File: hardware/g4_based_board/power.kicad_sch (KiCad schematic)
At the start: 10 parts, among them U2 AZ1117-3.3

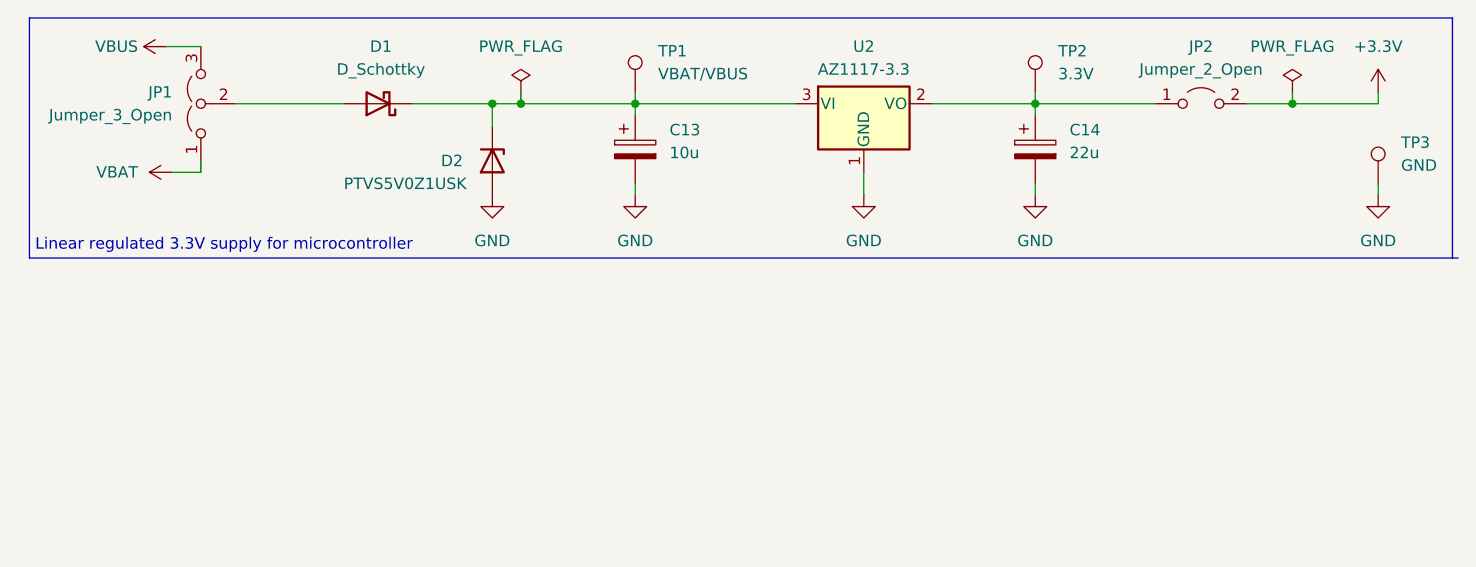
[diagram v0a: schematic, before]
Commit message: added a 5v linear reg
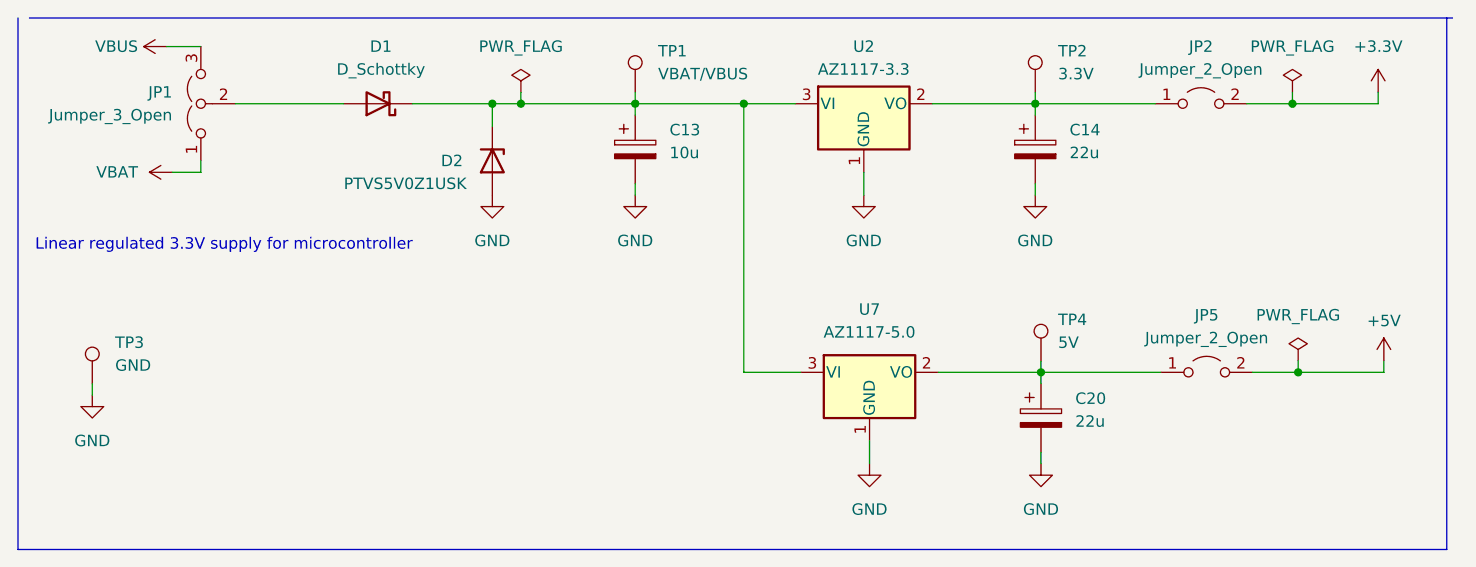
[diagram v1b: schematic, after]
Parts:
- added C20: 22u, Capacitor_SMD:C_0805_2012Metric, symbol Device:C_Polarized
- added JP5: Jumper_2_Open, symbol Jumper:Jumper_2_Open
- added TP4: 5V, TestPoint:TestPoint_Pad_D1.5mm, symbol Connector:TestPoint
- added U7: AZ1117-5.0, symbol Regulator_Linear:AZ1117-5.0
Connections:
- net GND: now also C20.2, U7.1 (GND)
- net at C13.1, D1.1 (K), D2.1 (K)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: now also U7.3 (VI)
- new net: C20.1, JP5.1 (A), TP4.1, U7.2 (VO)
- new net +5V: JP5.2 (B)
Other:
- moved on the sheet: TP3

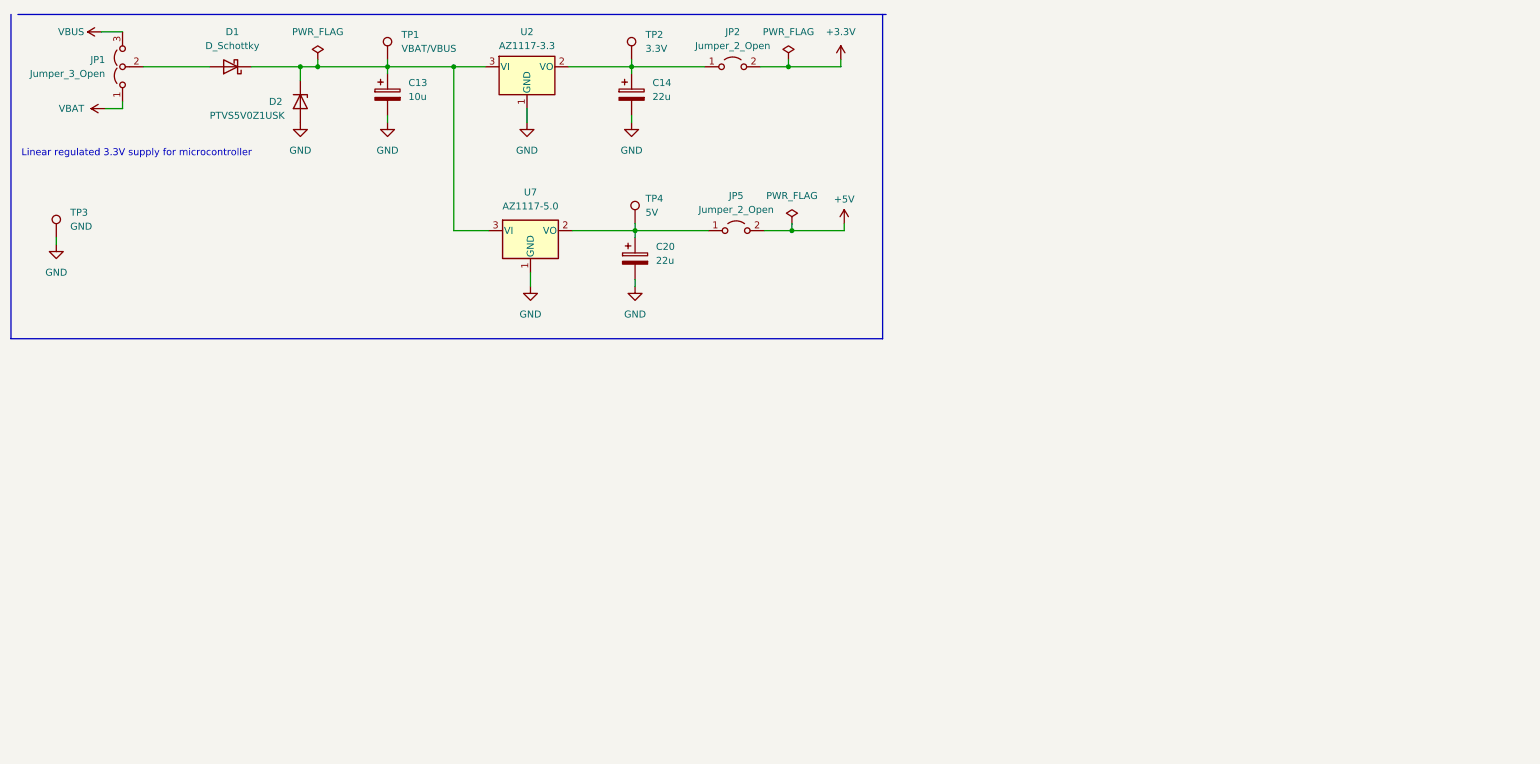
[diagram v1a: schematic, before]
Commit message: moved the 5v reg to only use the battery as input
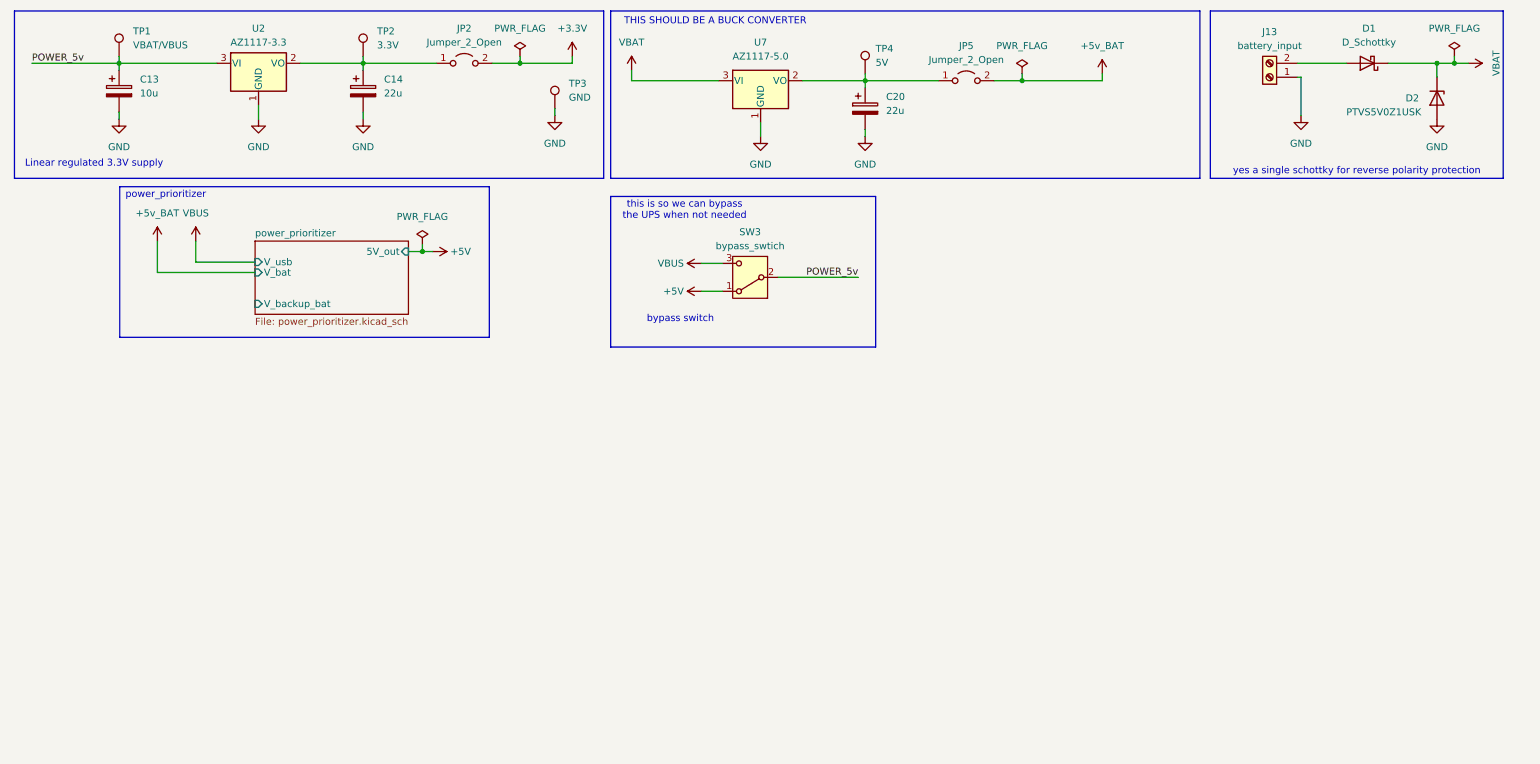
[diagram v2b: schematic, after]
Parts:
- removed JP1: Jumper_3_Open, Connector_PinHeader_2.54mm:PinHeader_1x03_P2.54mm_Vertical, symbol Jumper:Jumper_3_Open
- added J13: battery_input, symbol Connector:Screw_Terminal_01x02
- added SW3: bypass_swtich, symbol Switch:SW_SPDT
- U7: footprint (none) -> Package_TO_SOT_SMD:SOT-223
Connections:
- net +5V: now also SW3.1 (A); no longer JP5.2 (B)
- net GND: now also J13.1 (Pin_1)
- net VBAT: now also D1.1 (K), D2.1 (K), U7.3 (VI)
- net VBUS: now also SW3.3 (C)
- net POWER_5v: now reaches C13.1, TP1.1, U2.3 (VI)
- net POWER_5v: now also SW3.2 (B); no longer D1.1 (K), D2.1 (K), U7.3 (VI)
- net at D1.2 (A): now also J13.2 (Pin_2)
- new net +5v_BAT: JP5.2 (B)
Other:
- added sheet power_prioritizer (power_prioritizer.kicad_sch)
- note added: "Linear regulated 3.3V supply"
- note added: "THIS SHOULD BE A BUCK CONVERTER"
- note added: "bypass switch"
- note added: "power_prioritizer"
- note added: "this is so we can bypass the UPS when not needed"
- note added: "yes a single schottky for reverse polarity protection"
- note removed: "Linear regulated 3.3V supply for microcontroller"
- moved on the sheet: C13, C14, JP2, TP1, TP2, TP3, U2

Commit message: changed power to be an external module
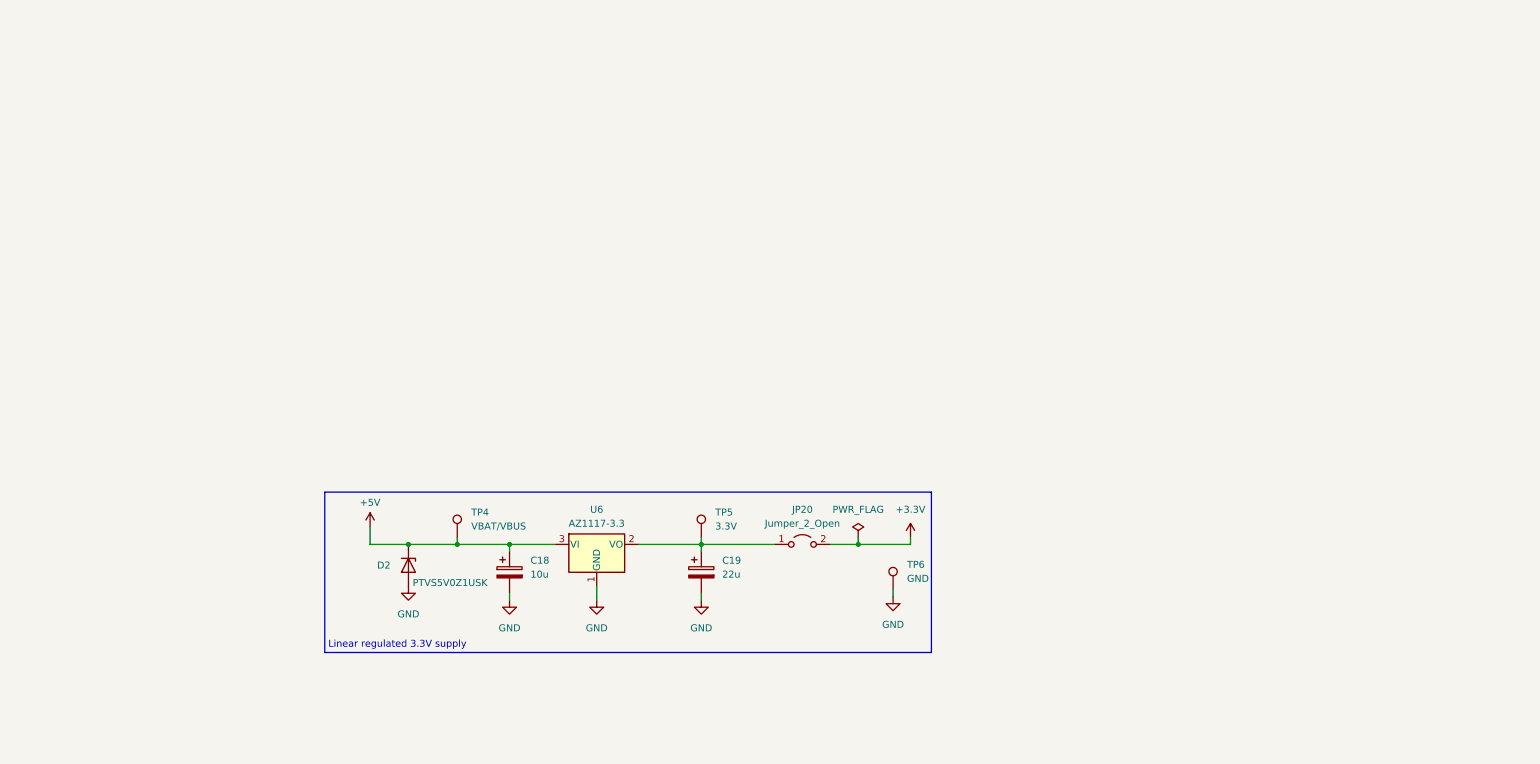
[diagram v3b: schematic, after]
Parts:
- removed C13: 10u, Capacitor_SMD:C_0805_2012Metric, symbol Device:C_Polarized
- removed C14, C20: 22u, Capacitor_SMD:C_0805_2012Metric, symbol Device:C_Polarized
- removed D1: D_Schottky, Diode_SMD:D_0805_2012Metric_Pad1.15x1.40mm_HandSolder, symbol Device:D_Schottky
- removed J13: battery_input, symbol Connector:Screw_Terminal_01x02
- removed JP2, JP5: Jumper_2_Open, symbol Jumper:Jumper_2_Open
- removed SW3: bypass_swtich, symbol Switch:SW_SPDT
- removed TP1: VBAT/VBUS, TestPoint:TestPoint_Pad_D1.5mm, symbol Connector:TestPoint
- removed TP2: 3.3V, TestPoint:TestPoint_Pad_D1.5mm, symbol Connector:TestPoint
- removed TP3: GND, TestPoint:TestPoint_Pad_D1.5mm, symbol Connector:TestPoint
- removed U2: AZ1117-3.3, Package_TO_SOT_SMD:SOT-223, symbol Regulator_Linear:AZ1117-3.3
- removed U7: AZ1117-5.0, Package_TO_SOT_SMD:SOT-223, symbol Regulator_Linear:AZ1117-5.0
- added C18: 10u, Capacitor_SMD:C_0603_1608Metric_Pad1.08x0.95mm_HandSolder, symbol Device:C_Polarized
- added C19: 22u, Capacitor_SMD:C_0603_1608Metric_Pad1.08x0.95mm_HandSolder, symbol Device:C_Polarized
- added JP20: Jumper_2_Open, Jumper:SolderJumper-2_P1.3mm_Open_TrianglePad1.0x1.5mm, symbol Jumper:Jumper_2_Open
- added TP5: 3.3V, TestPoint:TestPoint_Pad_D1.5mm, symbol Connector:TestPoint
- added TP6: GND, TestPoint:TestPoint_Pad_D1.5mm, symbol Connector:TestPoint
- added U6: AZ1117-3.3, Package_TO_SOT_SMD:SOT-223, symbol Regulator_Linear:AZ1117-3.3
- TP4: value 5V -> VBAT/VBUS
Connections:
- net VBAT is gone; now on net +5V: D2.1 (K)
- net +3.3V: now also JP20.2 (B)
- net +5V: now also TP4.1, C18.1, U6.3 (VI)
- net GND: now also C18.2, C19.2, TP6.1, U6.1 (GND)
- new net: C19.1, JP20.1 (A), TP5.1, U6.2 (VO)
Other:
- removed sheet power_prioritizer
- note removed: "THIS SHOULD BE A BUCK CONVERTER"
- note removed: "bypass switch"
- note removed: "power_prioritizer"
- note removed: "this is so we can bypass the UPS when not needed"
- note removed: "yes a single schottky for reverse polarity protection"

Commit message: added the tps2117 to swap between usb power and power supply power
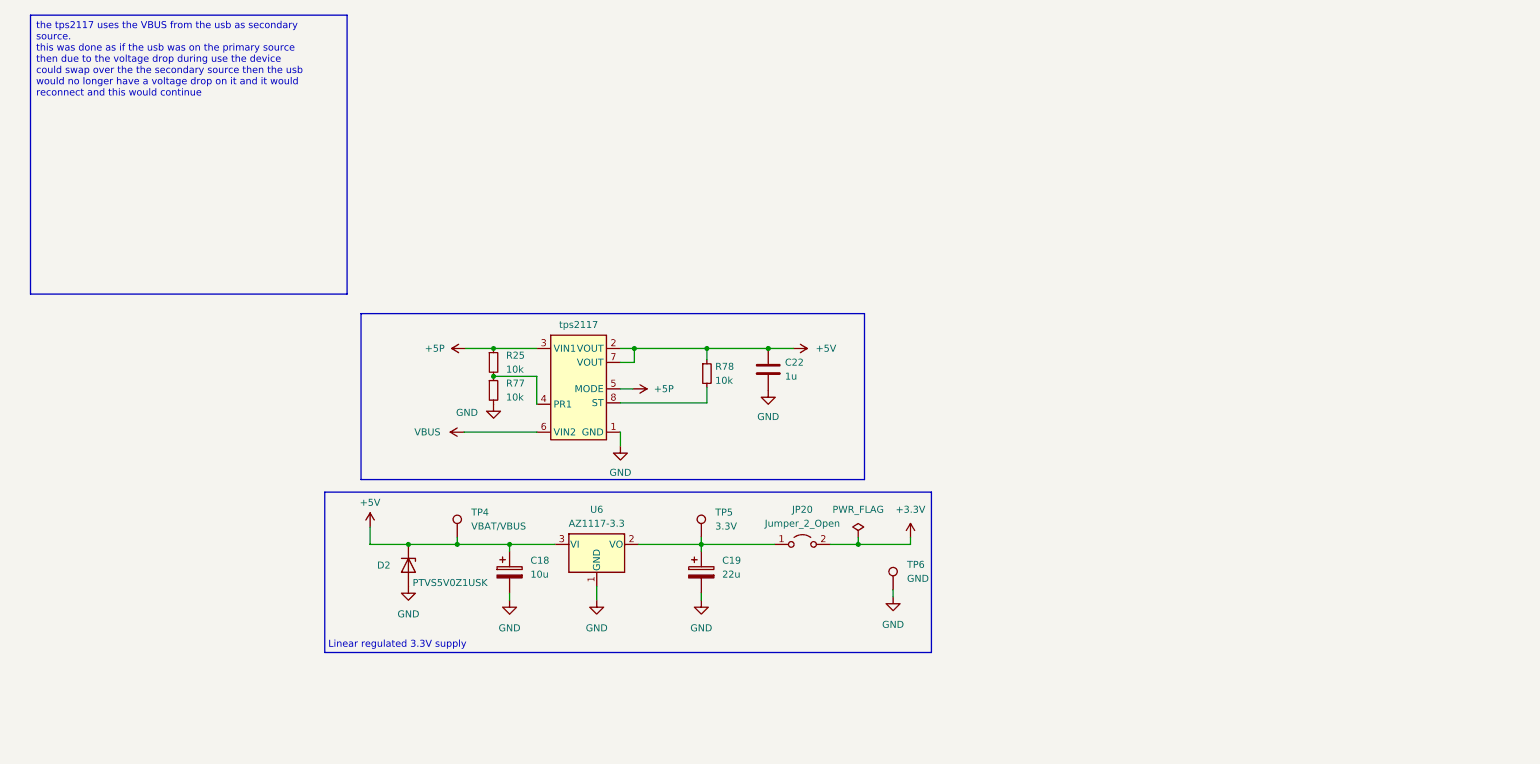
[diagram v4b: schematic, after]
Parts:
- added C22: 1u, symbol Device:C
- added R25, R77, R78: 10k, symbol Device:R_Small
- added U1: tps2117, symbol parts_not_in_kicad:TPS2117
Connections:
- net +5V: now also C22.1, R78.1, U1.2 (VOUT), U1.7 (VOUT)
- net GND: now also C22.2, R77.2, U1.1 (GND)
- new net: R25.2, R77.1, U1.4 (PR1)
- new net: R78.2, U1.8 (ST)
- new net +5P: R25.1, U1.3 (VIN1), U1.5 (MODE)
- new net VBUS: U1.6 (VIN2)

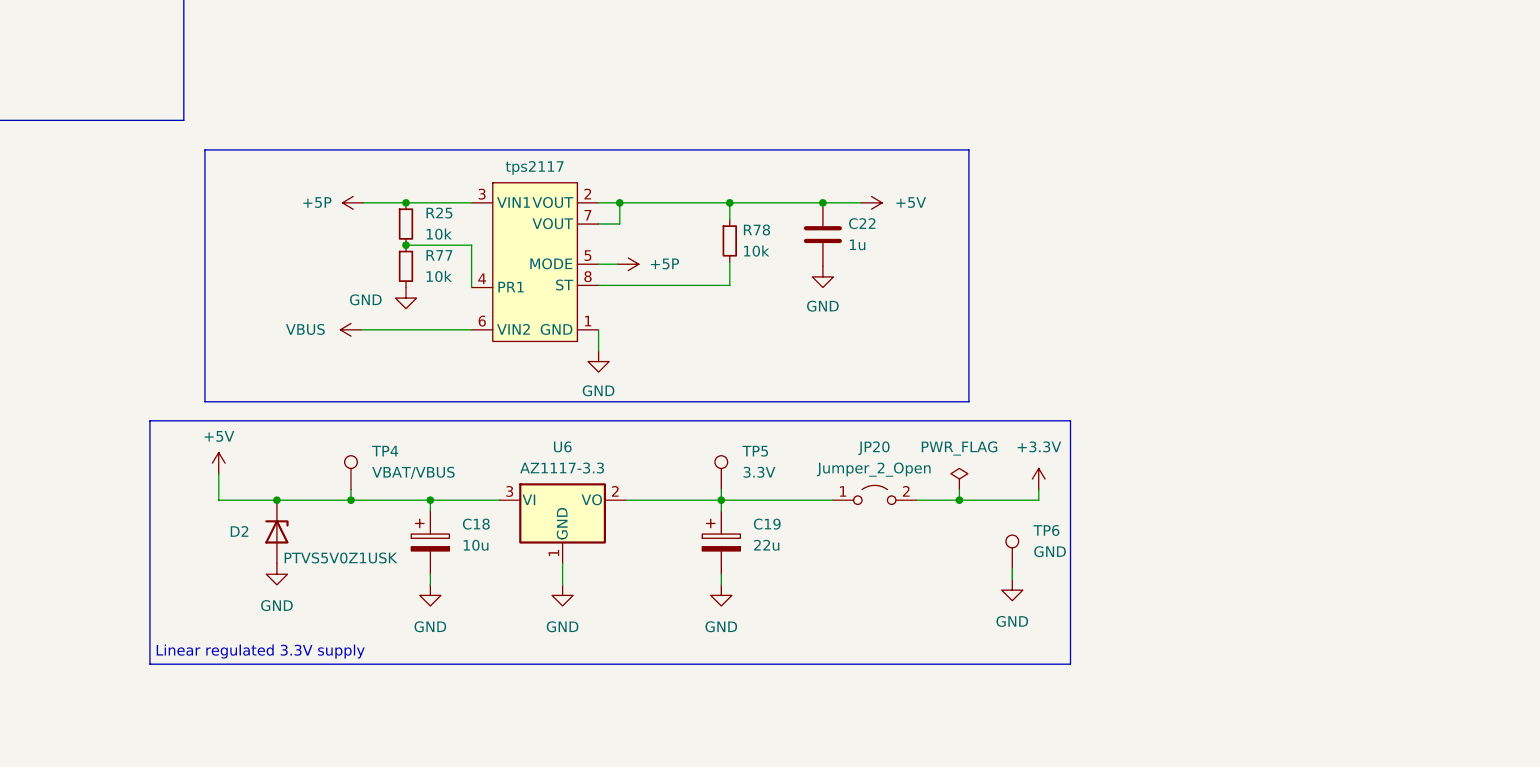
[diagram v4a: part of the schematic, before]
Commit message: added power signal for mcu to know what power source its using
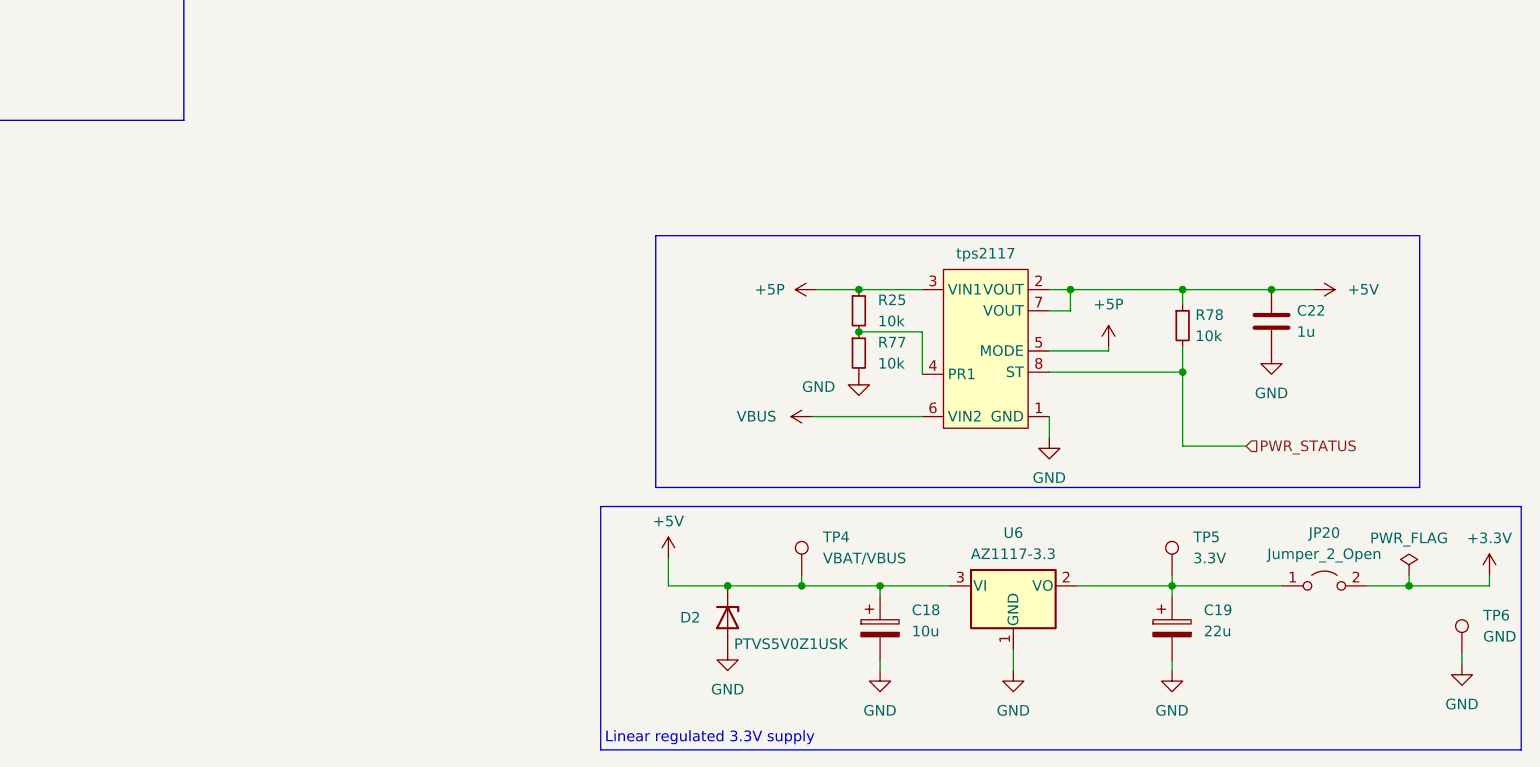
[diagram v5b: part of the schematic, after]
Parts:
- C22: footprint (none) -> Capacitor_SMD:C_0603_1608Metric_Pad1.08x0.95mm_HandSolder
- R25, R77, R78: footprint (none) -> Resistor_SMD:R_0603_1608Metric_Pad0.98x0.95mm_HandSolder
- U1: footprint (none) -> Package_TO_SOT_SMD:SOT-583-8
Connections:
- net PWR_STATUS: now reaches R78.2, U1.8 (ST)
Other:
- moved on the sheet: C18, C19, C22, D2, JP20, R25, R77, R78, TP4, TP5, TP6, U6
